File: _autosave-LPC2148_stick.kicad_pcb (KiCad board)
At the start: 2 copper layers, 132 x 51 mm, 73 parts, among them CON1 BARREL_JACK, CON2 USB-MINI-B, IC1 LM1117, IC2 LM1117, P1 CONN_01X40, P2 JTAG, P3 CONN_01X40, P4 USB Operation Selection, Q1 BC856, SW1 RST, SW2 Power, SW3 ISP, SW4 ISP, SW5 User Sw1, U1 LPC2148, X1 3.768KHz, X2 12MHz

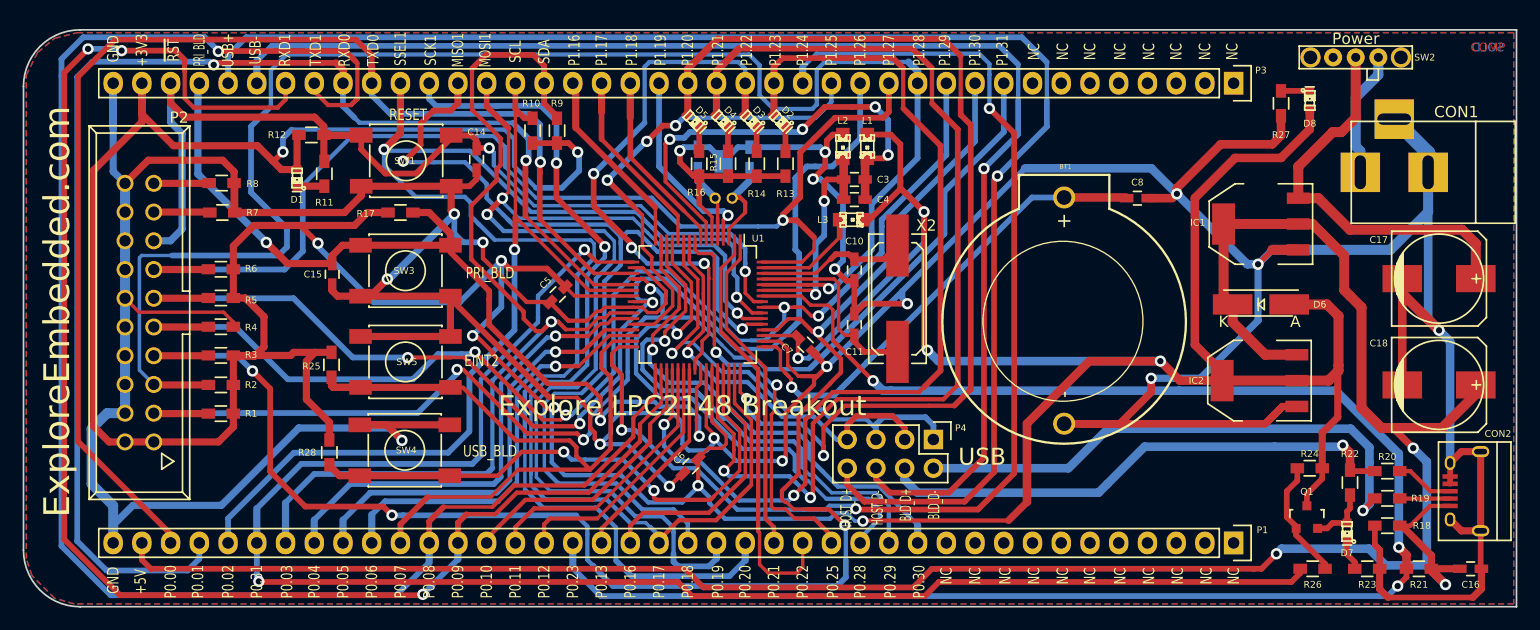
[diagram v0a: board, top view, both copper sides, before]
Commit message: Legend modified
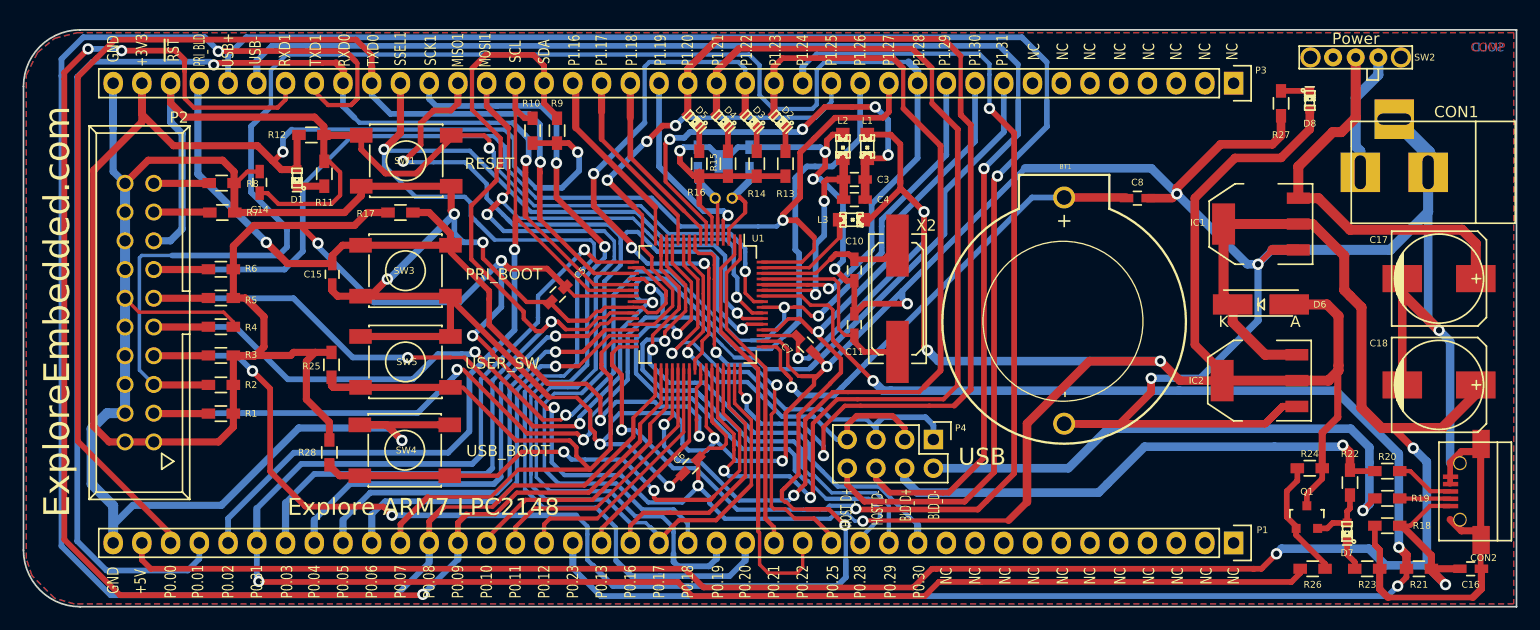
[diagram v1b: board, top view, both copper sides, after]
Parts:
- CON2: footprint Connect:USB_Micro-B -> EE:USB_Micro-B_SMD
- moved C14 19.3 mm to (79.9, 54.5), turned to 270 degrees
- moved CON2 2.02 mm to (185.2, 83.1), turned to 180 degrees
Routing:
- net /~RST: track 90.8 -> 100.0 mm
- net GND: track 658.7 -> 658.1 mm
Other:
- board text added: "Explore ARM7 LPC2148"
- board text added: "PRI_BOOT"
- board text added: "USB_BOOT"
- board text added: "USER_SW"
- board text removed: "EINT2"
- board text removed: "Explore LPC2148 Breakout"
- board text removed: "USB_BLD"
